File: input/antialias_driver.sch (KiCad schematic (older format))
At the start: 21 parts, among them U103 LT1028, U104 THS4131

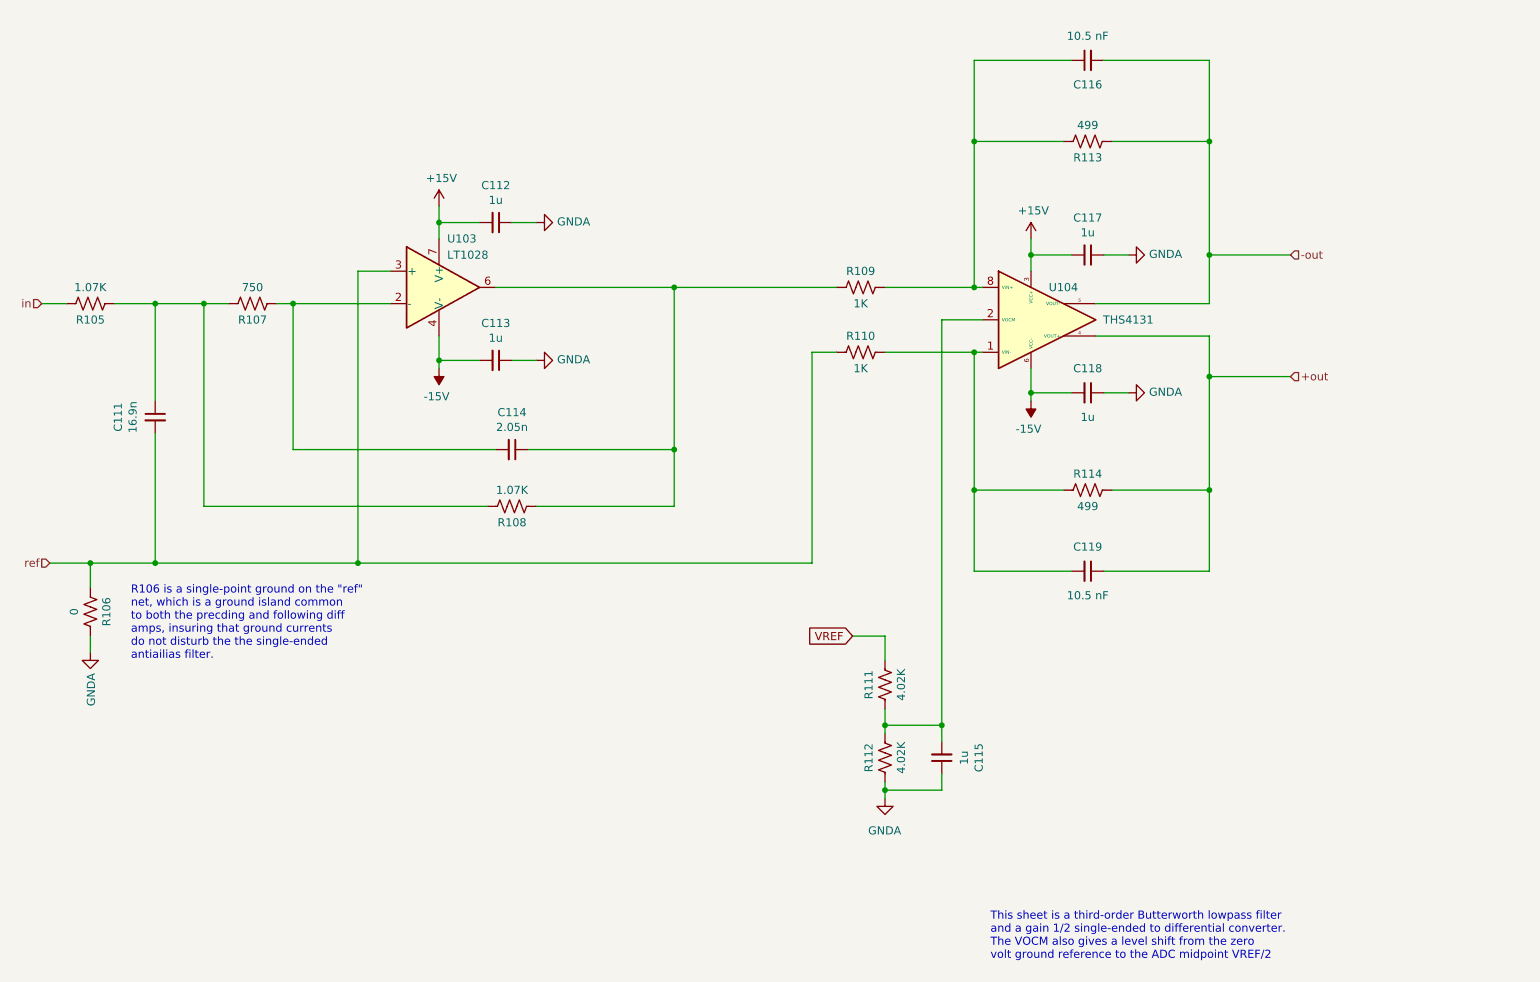
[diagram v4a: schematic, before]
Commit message: Still beating into overall shape.  This is a checkpoint before modifying the analog signal chain to fold the diff amp and antialias into the driver, going to a full differential path.
Overall: Changes to component attributes to reduce duplicates in BOM, and added links to Digikey and datasheets.

board_connector.sch: Added reference input pins, decimation SEL lines.

in_filter.sch:
Fixed BIST feedback to be taken at the top of each injection resistor (4 lines, not 2)

input_board.sch:
Added some missing connections and no-connects.

power_budget.xlsx:
Much more elaborate now, models effect of input levels on load currents, computes currents and total power, for several variants.

reference_buffer.sch:
Updated with booster sink transistor to handle sourcing into reference by ADC clamp diodes.

simetrix/:
Added supply_negative.wxsch and supply_positive.wxsch, which are concepts for low noise lowish dropout regulators for the analog rails.  Other simetrix modifications are cosmetic.
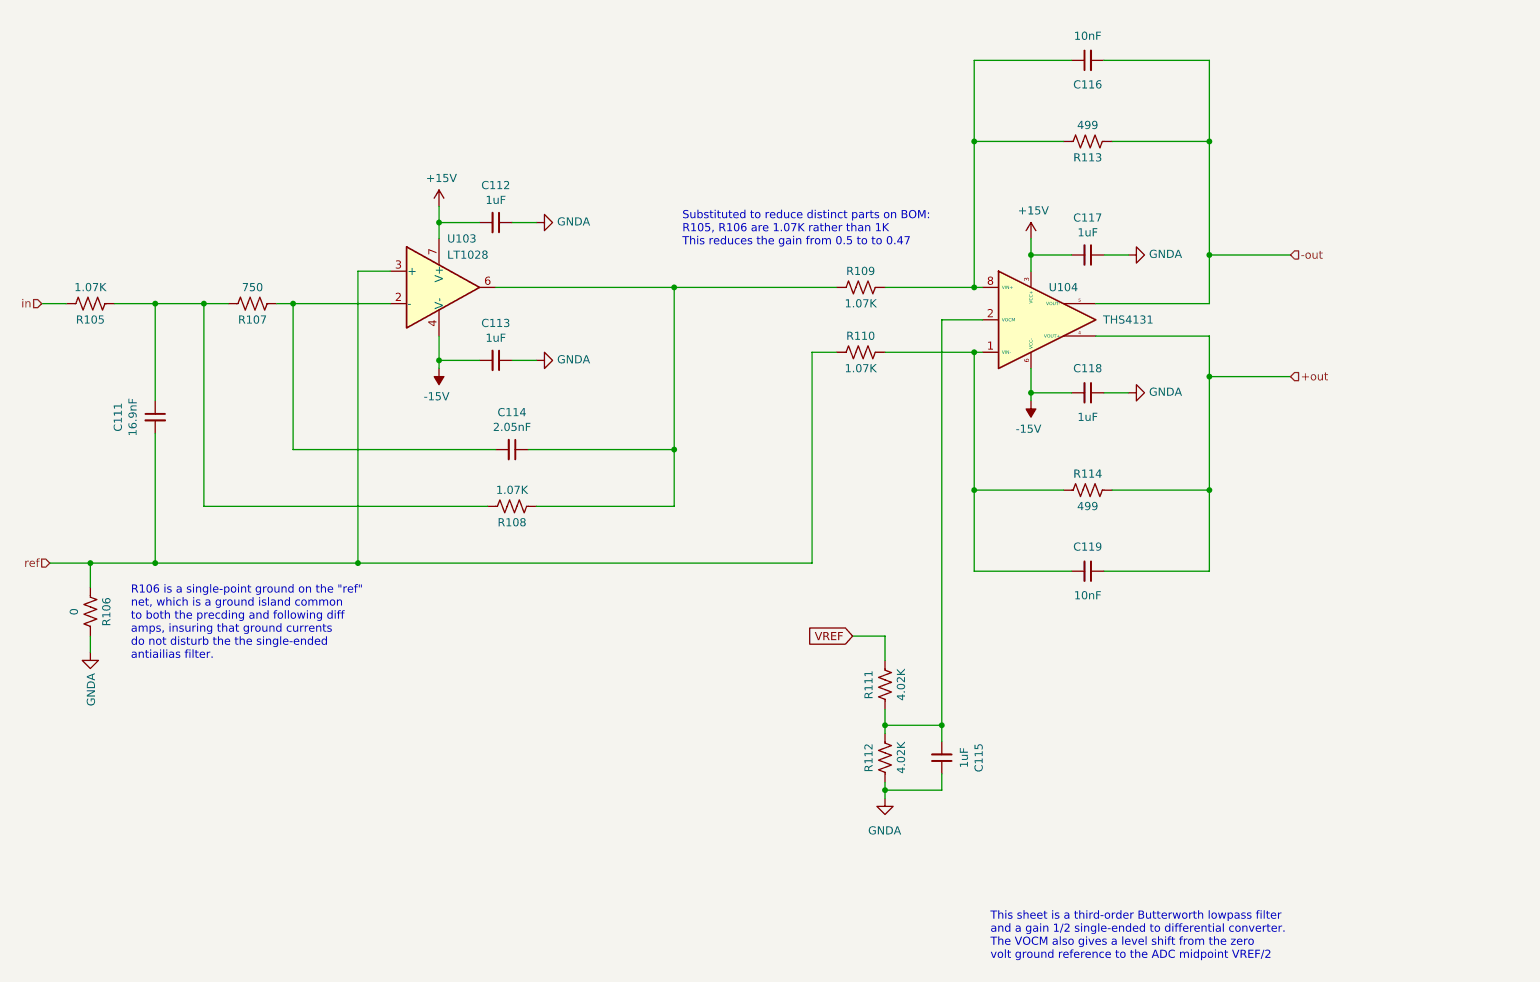
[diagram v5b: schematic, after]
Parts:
- C111: value 16.9n -> 16.9nF
- C112, C113, C115, C117, C118: value 1u -> 1uF
- C114: value 2.05n -> 2.05nF
- C116, C119: value 10.5 nF -> 10nF; Description (none) -> CAP CER 10000PF 50V C0G/NP0 0805; Digikey (none) -> 490-8296-1-ND; MPN (none) -> GRM2195C1H103GA01D; Notes (none) -> 2% C0G
- R109, R110: value 1K -> 1.07K
- R111, R112: footprint Resistor_SMD:R_0603_1608Metric -> Resistor_SMD:R_0805_2012Metric; Notes (none) -> 0.1%
- R113, R114: footprint Resistor_SMD:R_0603_1608Metric -> Resistor_SMD:R_1206_3216Metric; Description (none) -> RES 499 OHM 0.1% 2/5W 1206; Digikey (none) -> 541-3877-1-ND
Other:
- note added: "Substituted to reduce distinct parts on BOM:\nR105, R106 are 1.07K rather than 1K \nThis reduces the gain from 0.5 to to 0.47"
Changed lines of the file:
@@
 P 7700 2600
 F 0 "C117" V 7471 2600 50  0000 C CNN
-F 1 "1u" V 7562 2600 50  0000 C CNN
+F 1 "1uF" V 7562 2600 50  0000 C CNN
 F 2 "Capacitor_SMD:C_0603_1608Metric" H 7700 2600 50  0001 C CNN
 F 3 "~" H 7700 2600 50  0001 C CNN
@@
 P 4050 3250
 F 0 "C113" V 3821 3250 50  0000 C CNN
-F 1 "1u" V 3912 3250 50  0000 C CNN
+F 1 "1uF" V 3912 3250 50  0000 C CNN
 F 2 "Capacitor_SMD:C_0603_1608Metric" H 4050 3250 50  0001 C CNN
 F 3 "~" H 4050 3250 50  0001 C CNN
@@
 P 4150 3800
 F 0 "C114" V 3921 3800 50  0000 C CNN
-F 1 "2.05n" V 4012 3800 50  0000 C CNN
+F 1 "2.05nF" V 4012 3800 50  0000 C CNN
 F 2 "Capacitor_SMD:C_0603_1608Metric" H 4150 3800 50  0001 C CNN
 F 3 "~" H 4150 3800 50  0001 C CNN
@@
 P 1950 3600
 F 0 "C111" V 1721 3600 50  0000 C CNN
-F 1 "16.9n" V 1812 3600 50  0000 C CNN
+F 1 "16.9nF" V 1812 3600 50  0000 C CNN
 F 2 "Capacitor_SMD:C_0603_1608Metric" H 1950 3600 50  0001 C CNN
 F 3 "~" H 1950 3600 50  0001 C CNN
@@
 F 0 "R111" V 6550 5250 50  0000 C CNN
 F 1 "4.02K" V 6350 5250 50  0000 C CNN
-F 2 "Resistor_SMD:R_0603_1608Metric" V 6490 5240 50  0001 C CNN
+F 2 "Resistor_SMD:R_0805_2012Metric" V 6490 5240 50  0001 C CNN
 F 3 "~" H 6450 5250 50  0001 C CNN
+F 4 "0.1%" H 6450 5250 50  0001 C CNN "Notes"
 	1    6450 5250
 	-1   0    0    1
@@
 F 0 "R112" V 6550 5700 50  0000 C CNN
 F 1 "4.02K" V 6350 5700 50  0000 C CNN
-F 2 "Resistor_SMD:R_0603_1608Metric" V 6490 5690 50  0001 C CNN
+F 2 "Resistor_SMD:R_0805_2012Metric" V 6490 5690 50  0001 C CNN
 F 3 "~" H 6450 5700 50  0001 C CNN
+F 4 "0.1%" H 6450 5700 50  0001 C CNN "Notes"
 	1    6450 5700
 	-1   0    0    1
@@
 P 6800 5700
 F 0 "C115" V 6571 5700 50  0000 C CNN
-F 1 "1u" V 6662 5700 50  0000 C CNN
+F 1 "1uF" V 6662 5700 50  0000 C CNN
 F 2 "Capacitor_SMD:C_0603_1608Metric" H 6800 5700 50  0001 C CNN
 F 3 "~" H 6800 5700 50  0001 C CNN
@@
 F 0 "R114" V 7800 4050 50  0000 C CNN
 F 1 "499" V 7600 4050 50  0000 C CNN
-F 2 "Resistor_SMD:R_0603_1608Metric" V 7740 4040 50  0001 C CNN
-F 3 "~" H 7700 4050 50  0001 C CNN
+F 2 "Resistor_SMD:R_1206_3216Metric" V 7740 4040 50  0001 C CNN
+F 3 "http://www.vishay.com/docs/28758/tnpw_e3.pdf" H 7700 4050 50  0001 C CNN
+F 4 "RES 499 OHM 0.1% 2/5W 1206" H 7700 4050 50  0001 C CNN "Description"
+F 5 "541-3877-1-ND" H 7700 4050 50  0001 C CNN "Digikey"
 	1    7700 4050
 	0    -1   -1   0
@@
 P 4050 2400
 F 0 "C112" V 3821 2400 50  0000 C CNN
-F 1 "1u" V 3912 2400 50  0000 C CNN
+F 1 "1uF" V 3912 2400 50  0000 C CNN
 F 2 "Capacitor_SMD:C_0603_1608Metric" H 4050 2400 50  0001 C CNN
 F 3 "~" H 4050 2400 50  0001 C CNN
@@
 P 7700 3450
 F 0 "C118" V 7550 3450 50  0000 C CNN
-F 1 "1u" V 7850 3450 50  0000 C CNN
+F 1 "1uF" V 7850 3450 50  0000 C CNN
 F 2 "Capacitor_SMD:C_0603_1608Metric" H 7700 3450 50  0001 C CNN
 F 3 "~" H 7700 3450 50  0001 C CNN
@@
 P 6300 2800
 F 0 "R109" V 6400 2800 50  0000 C CNN
-F 1 "1K" V 6200 2800 50  0000 C CNN
+F 1 "1.07K" V 6200 2800 50  0000 C CNN
 F 2 "Resistor_SMD:R_0603_1608Metric" V 6340 2790 50  0001 C CNN
 F 3 "~" H 6300 2800 50  0001 C CNN
@@
 P 6300 3200
 F 0 "R110" V 6400 3200 50  0000 C CNN
-F 1 "1K" V 6200 3200 50  0000 C CNN
+F 1 "1.07K" V 6200 3200 50  0000 C CNN
 F 2 "Resistor_SMD:R_0603_1608Metric" V 6340 3190 50  0001 C CNN
 F 3 "~" H 6300 3200 50  0001 C CNN
@@
 P 7700 4550
 F 0 "C119" V 7550 4550 50  0000 C CNN
-F 1 "10.5 nF" V 7850 4550 50  0000 C CNN
+F 1 "10nF" V 7850 4550 50  0000 C CNN
 F 2 "Capacitor_SMD:C_0805_2012Metric" H 7700 4550 50  0001 C CNN
 F 3 "~" H 7700 4550 50  0001 C CNN
+F 4 "2% C0G" H 7700 4550 50  0001 C CNN "Notes"
+F 5 "CAP CER 10000PF 50V C0G/NP0 0805" H 7700 4550 50  0001 C CNN "Description"
+F 6 "490-8296-1-ND" H 7700 4550 50  0001 C CNN "Digikey"
+F 7 "GRM2195C1H103GA01D" H 7700 4550 50  0001 C CNN "MPN"
 	1    7700 4550
 	0    1    1    0
@@
 F 0 "R113" V 7800 1900 50  0000 C CNN
 F 1 "499" V 7600 1900 50  0000 C CNN
-F 2 "Resistor_SMD:R_0603_1608Metric" V 7740 1890 50  0001 C CNN
-F 3 "~" H 7700 1900 50  0001 C CNN
+F 2 "Resistor_SMD:R_1206_3216Metric" V 7740 1890 50  0001 C CNN
+F 3 "http://www.vishay.com/docs/28758/tnpw_e3.pdf" H 7700 1900 50  0001 C CNN
+F 4 "RES 499 OHM 0.1% 2/5W 1206" H 7700 1900 50  0001 C CNN "Description"
+F 5 "541-3877-1-ND" H 7700 1900 50  0001 C CNN "Digikey"
 	1    7700 1900
 	0    1    1    0
@@
 P 7700 1400
 F 0 "C116" V 7550 1400 50  0000 C CNN
-F 1 "10.5 nF" V 7850 1400 50  0000 C CNN
+F 1 "10nF" V 7850 1400 50  0000 C CNN
 F 2 "Capacitor_SMD:C_0805_2012Metric" H 7700 1400 50  0001 C CNN
 F 3 "~" H 7700 1400 50  0001 C CNN
+F 4 "2% C0G" H 7700 1400 50  0001 C CNN "Notes"
+F 5 "CAP CER 10000PF 50V C0G/NP0 0805" H 7700 1400 50  0001 C CNN "Description"
+F 6 "490-8296-1-ND" H 7700 1400 50  0001 C CNN "Digikey"
+F 7 "GRM2195C1H103GA01D" H 7700 1400 50  0001 C CNN "MPN"
 	1    7700 1400
 	0    -1   -1   0
@@
 Text Notes 1800 5100 0    50   ~ 0
 R106 is a single-point ground on the "ref" \nnet, which is a ground island common\nto both the precding and following diff\namps, insuring that ground currents\ndo not disturb the the single-ended\nantiailias filter.
+Text Notes 5200 2550 0    50   ~ 0
+Substituted to reduce distinct parts on BOM:\nR105, R106 are 1.07K rather than 1K \nThis reduces the gain from 0.5 to to 0.47
 $EndSCHEMATC

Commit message: Changes mostly related to avoiding excess power consumption.  This is mainly by limiting the signal swing to 0..5V and using asymmetric supplies of -4V and +8V.  (Perhaps we can reduce these to 3/7 V.)  Also, I got rid of two stages in the input signal path.
power_budget.xlsx
power.sch
reference_buffer.sch:
Changes related to the new supply voltages, and start on the power supply section.

input_channel.sch
in_amp.sch
antialias_driver.sch:
Reworked the input signal chain to keep a full differential path, rolling the antialias filter
into the ADC driver.  Also, related to change to lower asymmetrical supply voltages, there is
no 20V PP anywhere (the this was for benefit of the antialias filter noise, but that stage is gone).  Also, added zener clamp on VREF in driver.

in_filter.sch: added missing DC bias resistors.
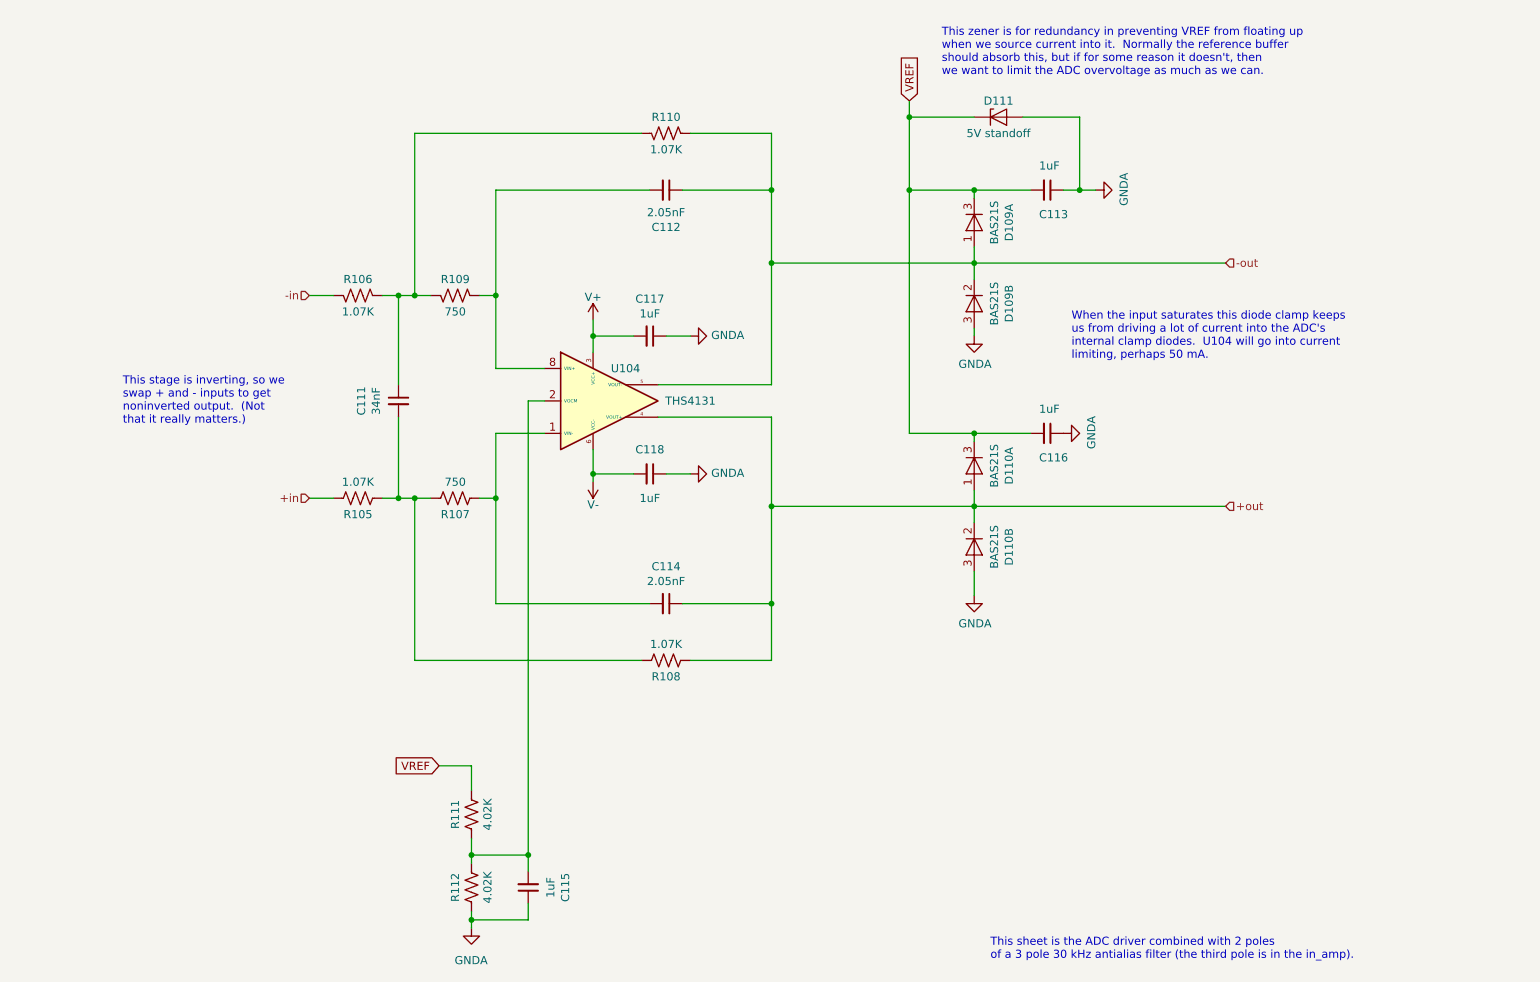
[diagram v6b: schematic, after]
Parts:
- removed C119: 10nF, Capacitor_SMD:C_0805_2012Metric, symbol Device:C_Small
- removed R113, R114: 499, Resistor_SMD:R_1206_3216Metric, symbol Device:R_US
- removed U103: LT1028, symbol ilemt_input:opamp_single
- added D109, D110: BAS21S, Package_TO_SOT_SMD:SOT-23, symbol Diode:BAV99
- added D111: 5V standoff, symbol Device:D_Zener
- C111: value 16.9nF -> 34nF
- C112: value 1uF -> 2.05nF
- C116: value 10nF -> 1uF; footprint Capacitor_SMD:C_0805_2012Metric -> Capacitor_SMD:C_0603_1608Metric; Description CAP CER 10000PF 50V C0G/NP0 0805 -> (none); Digikey 490-8296-1-ND -> (none); MPN GRM2195C1H103GA01D -> (none); Notes 2% C0G -> (none)
- R106: value 0 -> 1.07K; footprint Resistor_SMD:R_1206_3216Metric -> Resistor_SMD:R_0603_1608Metric
- R109: value 1.07K -> 750
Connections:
- net +out: now also C114.1, R108.1, D110.1 (A), D110.2 (K)
- net -out: now also C112.1, R110.1, D109.1 (A), D109.2 (K); no longer C116.2
- net GNDA: now also C116.1, D109.3 (A), D110.3 (A), D111.2 (A); no longer C112.1, R106.2
- net VREF: now also C113.2, C116.2, D109.3 (K), D110.3 (K), D111.1 (K)
- net at C114.2, R107.1: now also U104.1 (VIN-)
- net at R105.1, R107.2, R108.2: now also C111.2; no longer C111.1
- net at R110.2: now also C111.1, R106.1, R109.2; no longer U104.1 (VIN-)
- net +15V renamed V+
- net V+: no longer C112.2
- net -15V renamed V-
- net V-: no longer C113.2
- net in renamed +in
- removed net ref: C111.2, R106.1, R110.1
- new net: C112.2, R109.1, U104.8 (VIN+)
- new net -in: R106.2
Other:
- note added: "This sheet is the ADC driver combined with 2 poles \nof a 3 pole 30 kHz antialias filter (the third pole is in the in_amp).\n"
- note added: "This stage is inverting, so we \nswap + and - inputs to get\nnoninverted output. (Not \nthat it really matters.)"
- note added: "This zener is for redundancy in preventing VREF from floating up\nwhen we source current into it. Normally the reference buffer\nshould absorb this, but if for some reason it doesn't, then\nwe want to limit the ADC overvoltage as much as we can."
- note added: "When the input saturates this diode clamp keeps \nus from driving a lot of current into the ADC's \ninternal clamp diodes. U104 will go into current\nlimiting, perhaps 50 mA."
- note removed: "R106 is a single-point ground on the "ref" \nnet, which is a ground island common\nto both the precding and following diff\namps, insuring that ground currents\ndo not disturb the the single-ended\nantiailias filter."
- note removed: "Substituted to reduce distinct parts on BOM:\nR105, R106 are 1.07K rather than 1K \nThis reduces the gain from 0.5 to to 0.47"
- note removed: "This sheet is a third-order Butterworth lowpass filter\nand a gain 1/2 single-ended to differential converter.\nThe VOCM also gives a level shift from the zero \nvolt ground reference to the ADC midpoint VREF/2"
- moved on the sheet: C111, C114, C115, C117, C118, R105, R107, R108, R111, R112, U104
